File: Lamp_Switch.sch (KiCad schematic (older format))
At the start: 11 parts

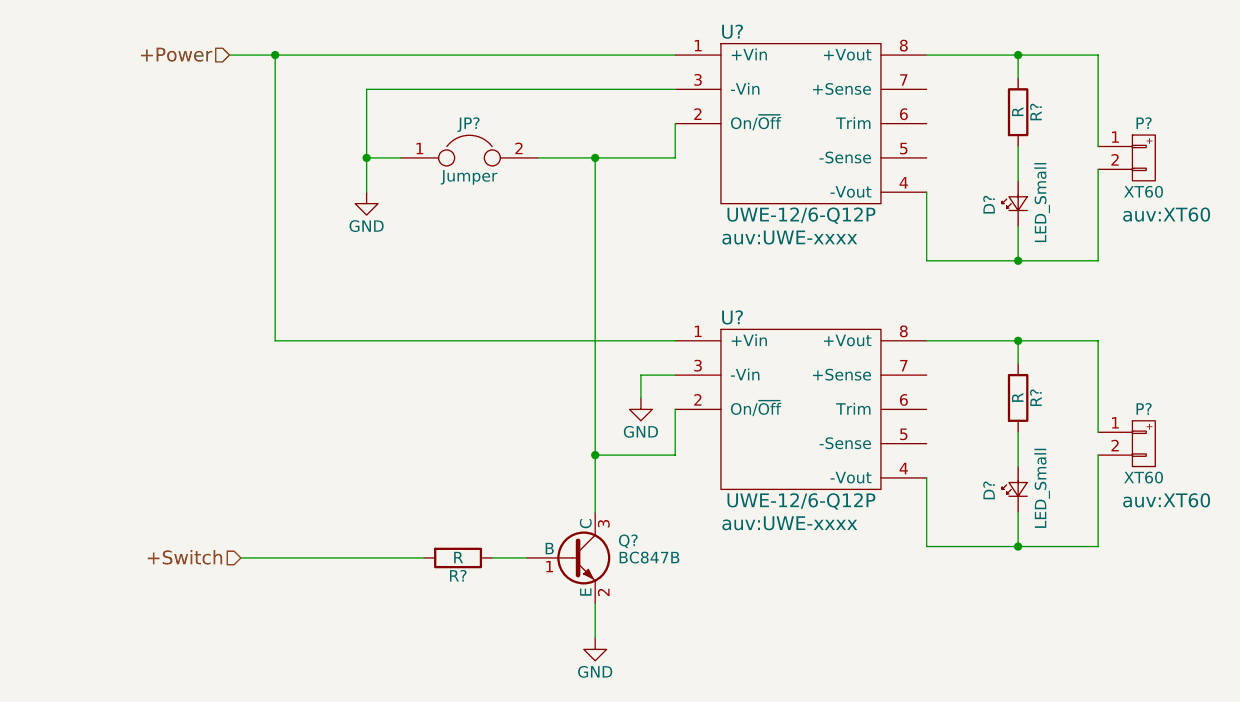
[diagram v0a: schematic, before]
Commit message: rename '+Switch' to 'Switch'
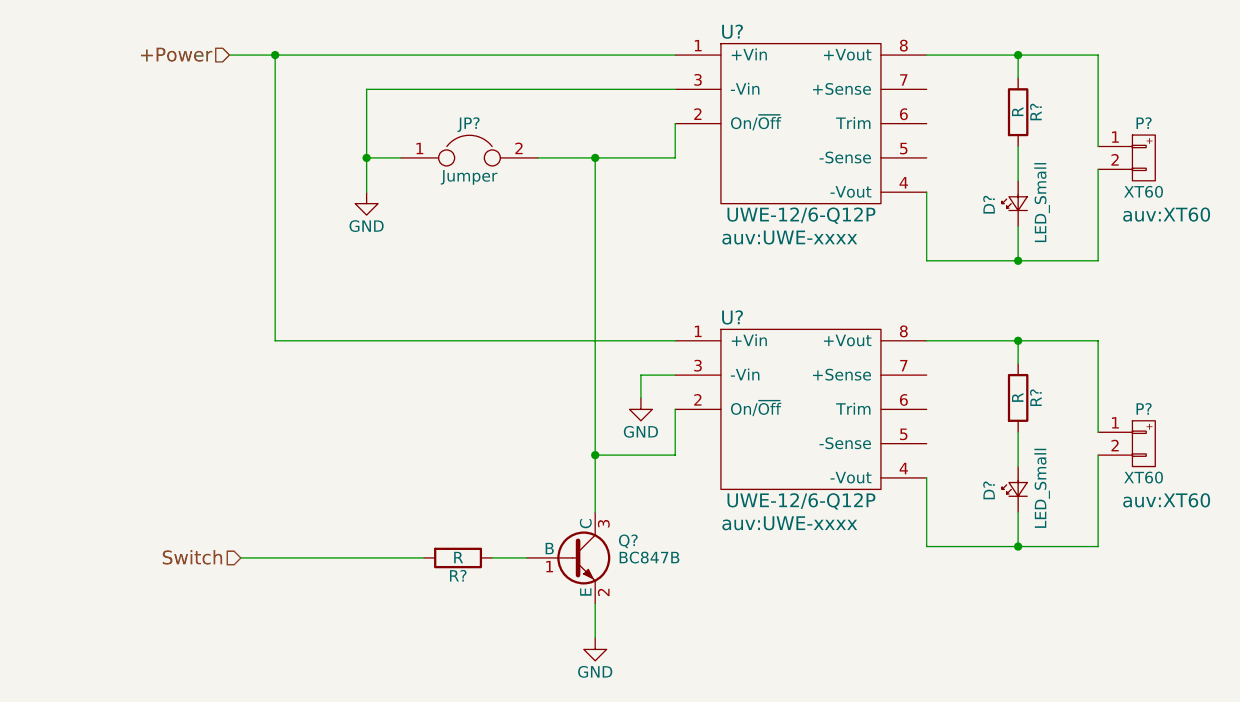
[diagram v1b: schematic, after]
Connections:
- net +Switch renamed Switch
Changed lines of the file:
@@
 +Power
 Text HLabel 3200 4800 0    60   Input ~ 0
-+Switch
+Switch
 $Comp
 L UWE-12/6-Q12P U?
@@
 	3750 2750 5100 2750
 Wire Wire Line
-	3750 2750 3750 3050
-Wire Wire Line
-	3750 3050 3750 3200
+	3750 2750 3750 3200
 Wire Wire Line
 	3900 3050 3750 3050
 Wire Wire Line
-	5100 3050 4750 3050
+	4500 3050 5100 3050
 Wire Wire Line
-	4750 3050 4500 3050
-Wire Wire Line
-	5100 2900 5100 3050
+	5100 3050 5100 2900
 Connection ~ 6600 3500
 Wire Wire Line
@@
 	6600 3500 6600 3350
 Wire Wire Line
-	6200 3500 6600 3500
-Wire Wire Line
-	6600 3500 6950 3500
+	6200 3500 6950 3500
 Wire Wire Line
 	6200 3200 6200 3500
@@
 	6600 2600 6600 2700
 Wire Wire Line
-	6200 2600 6600 2600
+	6200 2600 6950 2600
 Wire Wire Line
-	6600 2600 6950 2600
-Wire Wire Line
-	3150 2600 3350 2600
-Wire Wire Line
-	3350 2600 5100 2600
+	3150 2600 5100 2600
 Wire Wire Line
 	3350 3850 3350 2600
@@
 	4000 4800 3200 4800
 Wire Wire Line
-	4750 3050 4750 4350
-Wire Wire Line
-	4750 4350 4750 4600
+	4750 3050 4750 4600
 Wire Wire Line
 	4750 4350 5100 4350
@@
 $EndComp
 Wire Wire Line
-	6200 3850 6600 3850
-Wire Wire Line
-	6600 3850 6950 3850
+	6200 3850 6950 3850
 Wire Wire Line
 	6600 3850 6600 3950
@@
 	6200 4450 6200 4750
 Wire Wire Line
-	6200 4750 6600 4750
-Wire Wire Line
-	6600 4750 6950 4750
+	6200 4750 6950 4750
 Wire Wire Line
 	6600 4750 6600 4600

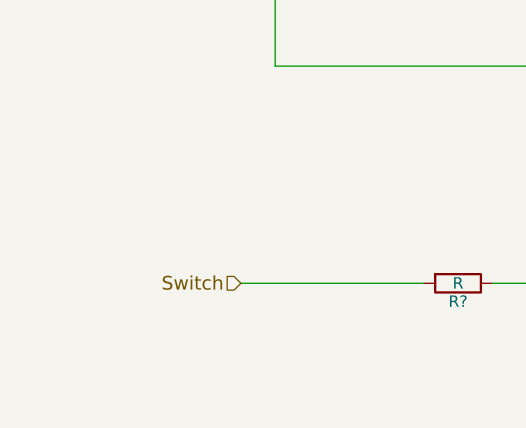
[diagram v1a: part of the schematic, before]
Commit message: change 'Switch' to 'Software_Switch'
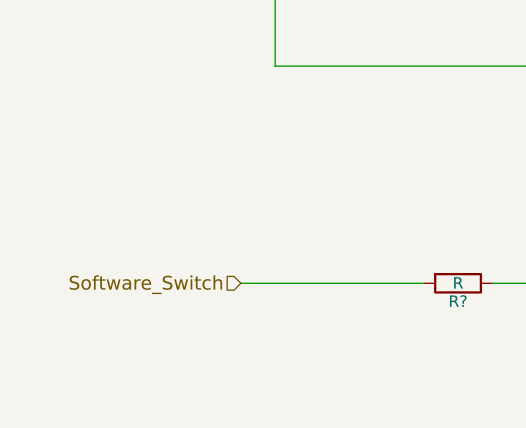
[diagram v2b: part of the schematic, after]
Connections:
- net Switch renamed Software_Switch
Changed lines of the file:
@@
 +Power
 Text HLabel 3200 4800 0    60   Input ~ 0
-Switch
+Software_Switch
 $Comp
 L UWE-12/6-Q12P U?

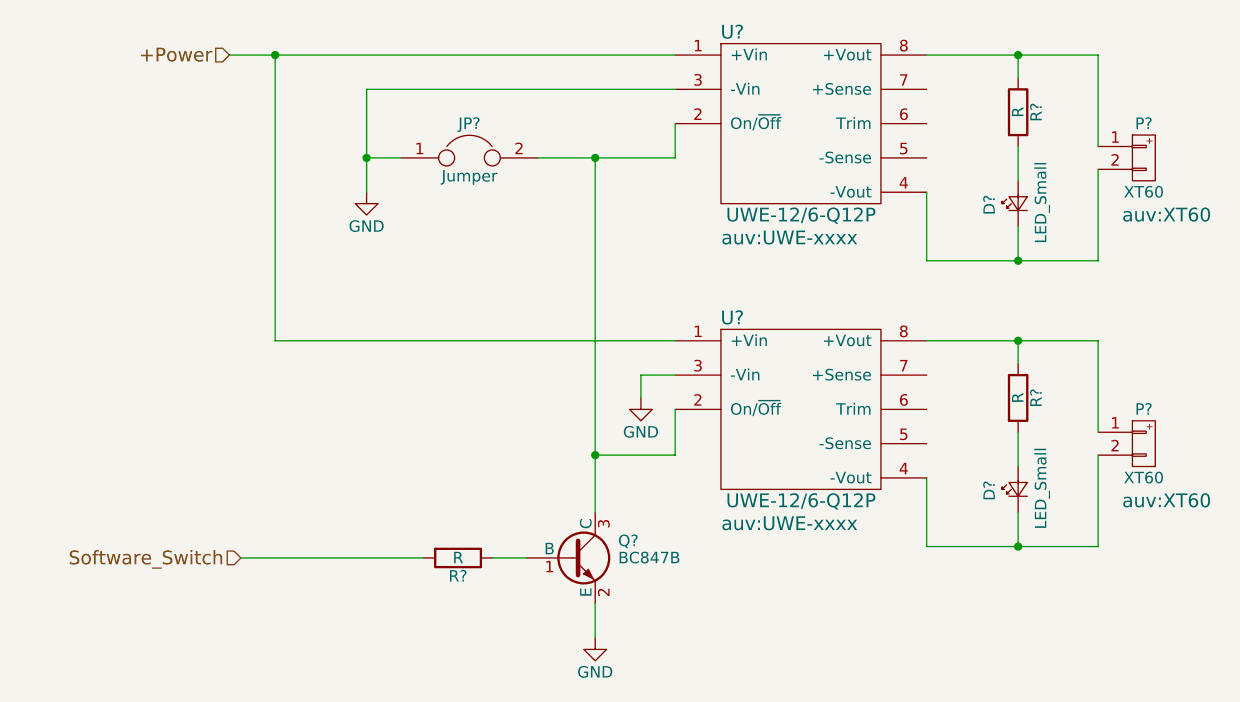
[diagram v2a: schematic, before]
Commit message: assign component value and change BC847B to BC817-40
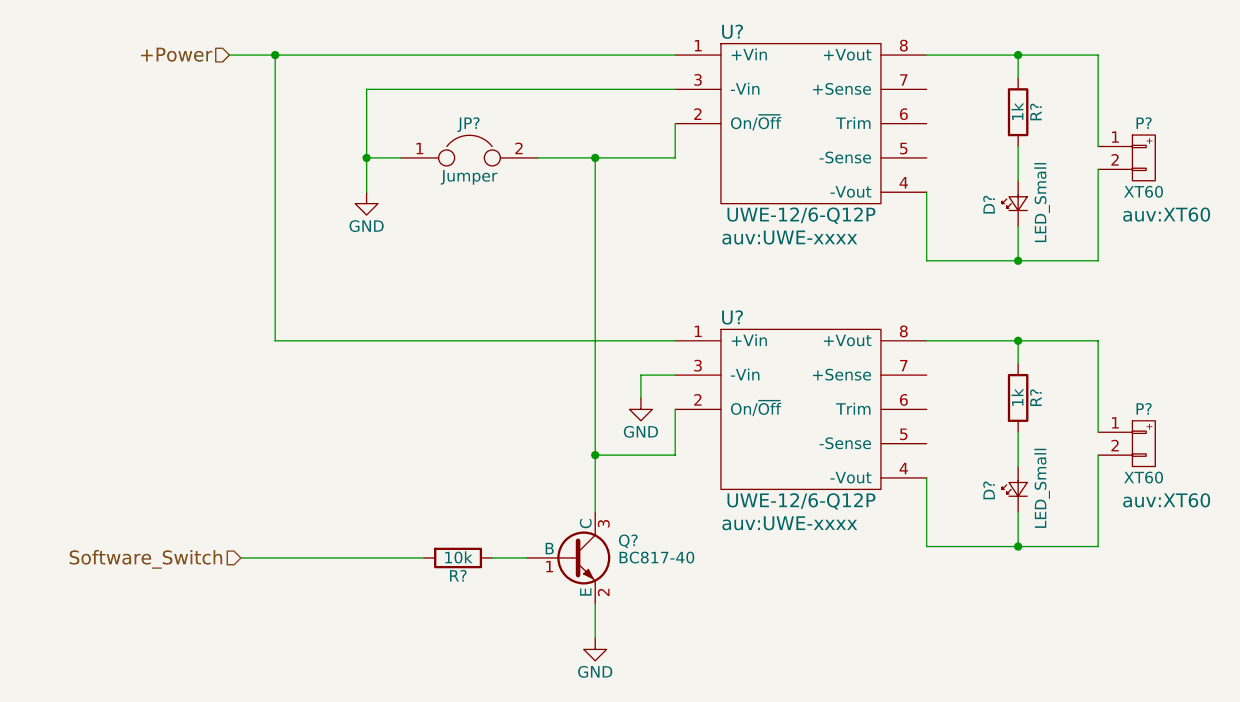
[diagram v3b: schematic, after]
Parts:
- removed Q?: BC847B, TO_SOT_Packages_SMD:SOT-23, symbol BC847B
- added Q?: BC817-40, TO_SOT_Packages_SMD:SOT-23, symbol BC817-40
- R? (x2): value R -> 1k
- R?: value R -> 10k
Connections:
- net GND: now also Q?.2 (E)
- net at JP?.2, U?.2 (On/~Off), U?.2 (On/~Off): now also Q?.3 (C)
- net at R?.1: now also Q?.1 (B)
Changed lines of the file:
@@
 P 6600 2850
 F 0 "R?" V 6680 2850 50  0000 C CNN
-F 1 "R" V 6600 2850 50  0000 C CNN
+F 1 "1k" V 6600 2850 50  0000 C CNN
 F 2 "Resistors_SMD:R_0603" V 6530 2850 50  0001 C CNN
 F 3 "" H 6600 2850 50  0001 C CNN
@@
 $EndComp
 $Comp
-L BC847B Q?
-U 1 1 58C99A5D
-P 4650 4800
-F 0 "Q?" H 4850 4875 50  0000 L CNN
-F 1 "BC847B" H 4850 4800 50  0000 L CNN
-F 2 "TO_SOT_Packages_SMD:SOT-23" H 4850 4725 50  0001 L CIN
-F 3 "" H 4650 4800 50  0001 L CNN
-	1    4650 4800
-	1    0    0    -1
-$EndComp
-$Comp
 L GND #PWR?
 U 1 1 58C99AB8
@@
 P 4150 4800
 F 0 "R?" V 4230 4800 50  0000 C CNN
-F 1 "R" V 4150 4800 50  0000 C CNN
+F 1 "10k" V 4150 4800 50  0000 C CNN
 F 2 "Resistors_SMD:R_0603" V 4080 4800 50  0001 C CNN
 F 3 "" H 4150 4800 50  0001 C CNN
@@
 P 6600 4100
 F 0 "R?" V 6680 4100 50  0000 C CNN
-F 1 "R" V 6600 4100 50  0000 C CNN
+F 1 "1k" V 6600 4100 50  0000 C CNN
 F 2 "Resistors_SMD:R_0603" V 6530 4100 50  0001 C CNN
 F 3 "" H 6600 4100 50  0001 C CNN
@@
 	6950 4750 6950 4350
 Connection ~ 6600 4750
+$Comp
+L BC817-40 Q?
+U 1 1 58E56DE9
+P 4650 4800
+F 0 "Q?" H 4850 4875 50  0000 L CNN
+F 1 "BC817-40" H 4850 4800 50  0000 L CNN
+F 2 "TO_SOT_Packages_SMD:SOT-23" H 4850 4725 50  0001 L CIN
+F 3 "" H 4650 4800 50  0001 L CNN
+	1    4650 4800
+	1    0    0    -1
+$EndComp
 $EndSCHEMATC
